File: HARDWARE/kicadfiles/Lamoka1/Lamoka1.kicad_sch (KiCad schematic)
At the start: 6 parts, among them J1 2606-1108/010-000, J2 2606-1352, J3 USB_C_Receptacle_USB2.0_14P, J4 470531000, J5 2604-1103

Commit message: General work on schem, BOM, footprints. Rout 11-14v to 5v buck converter
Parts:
- J3: Manufacturer HRO Electronics -> (none)
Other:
- note added: "This is the output of the transformer,"
- note added: "we will be hooking it up to a NEMA 5-15 plug."
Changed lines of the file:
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@@
 	(rectangle
 		(start 233.426 86.36)
-		(end 279.4 112.522)
+		(end 281.94 118.364)
 		(stroke
 			(width 0)
@@
 		)
 	)
+	(text "This is the output of the transformer, "
+		(exclude_from_sim no)
+		(at 253.238 114.3 0)
+		(effects
+			(font
+				(size 1.27 1.27)
+			)
+		)
+	)
 	(text "Wago-connector 2606-1108/010-000"
 		(exclude_from_sim no)
@@
 		(exclude_from_sim no)
 		(at 152.908 35.814 0)
+		(effects
+			(font
+				(size 1.27 1.27)
+			)
+		)
+	)
+	(text "we will be hooking it up to a NEMA 5-15 plug."
+		(exclude_from_sim no)
+		(at 257.81 116.332 0)
 		(effects
 			(font
@@
 		)
 		(property "Description" ""
+			(at 228.6 54.61 0)
+			(hide yes)
+			(show_name no)
+			(do_not_autoplace no)
+			(effects
+				(font
+					(size 1.27 1.27)
+				)
+			)
+		)
+		(property "KLC_S4.2_DVDD" ""
+			(at 228.6 54.61 0)
+			(hide yes)
+			(show_name no)
+			(do_not_autoplace no)
+			(effects
+				(font
+					(size 1.27 1.27)
+				)
+			)
+		)
+		(property "KLC_S4.2_VREG_LX" ""
 			(at 228.6 54.61 0)
 			(hide yes)
@@
 			)
 		)
-		(property "Manufacturer" "HRO Electronics"
-			(at 29.21 107.95 0)
-			(hide yes)
-			(show_name no)
-			(do_not_autoplace no)
-			(effects
-				(font
-					(size 1.27 1.27)
-				)
-			)
-		)
-		(property "Notes" ""
-			(at 29.21 107.95 0)
-			(hide yes)
-			(show_name no)
-			(do_not_autoplace no)
-			(effects
-				(font
-					(size 1.27 1.27)
-				)
-			)
-		)
 		(property "KLC_S4.2_DVDD" ""
 			(at 29.21 107.95 0)
@@
 			(at 142.24 68.58 0)
 			(hide yes)
+			(show_name no)
+			(do_not_autoplace no)
+			(effects
+				(font
+					(size 1.27 1.27)
+				)
+			)
+		)
+		(property "KLC_S4.2_DVDD" ""
+			(at 142.24 68.58 0)
+			(hide yes)
+			(show_name no)
+			(do_not_autoplace no)
+			(effects
+				(font
+					(size 1.27 1.27)
+				)
+			)
+		)
+		(property "KLC_S4.2_VREG_LX" ""
+			(at 142.24 68.58 0)
+			(hide yes)

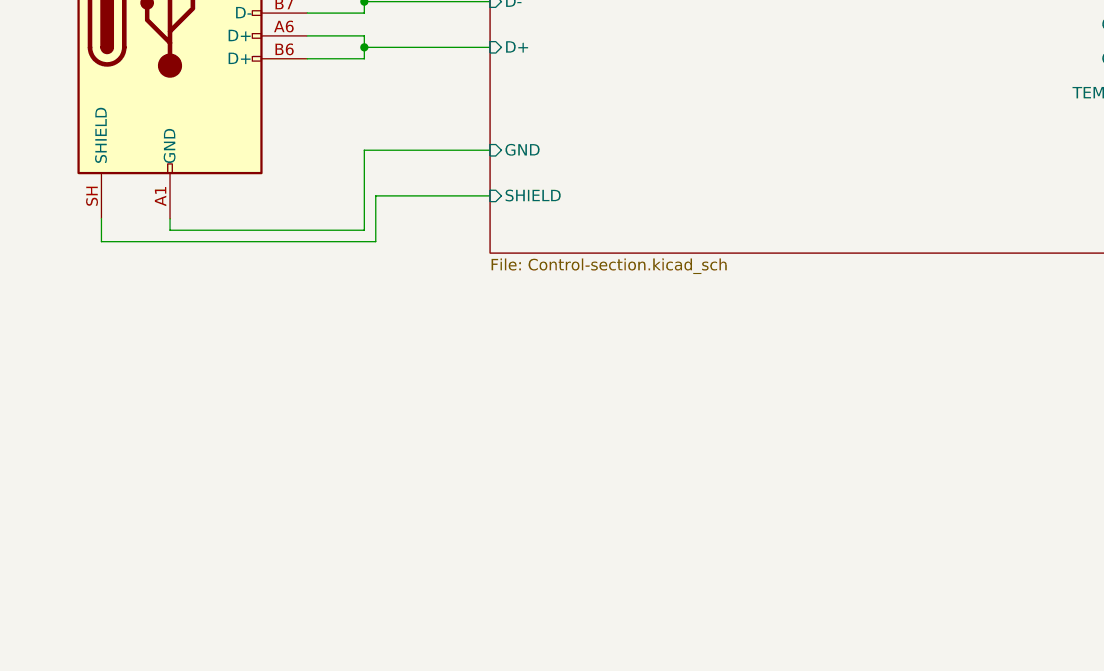
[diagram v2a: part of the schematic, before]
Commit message: ADD seperate user interface board, improve doccumentation
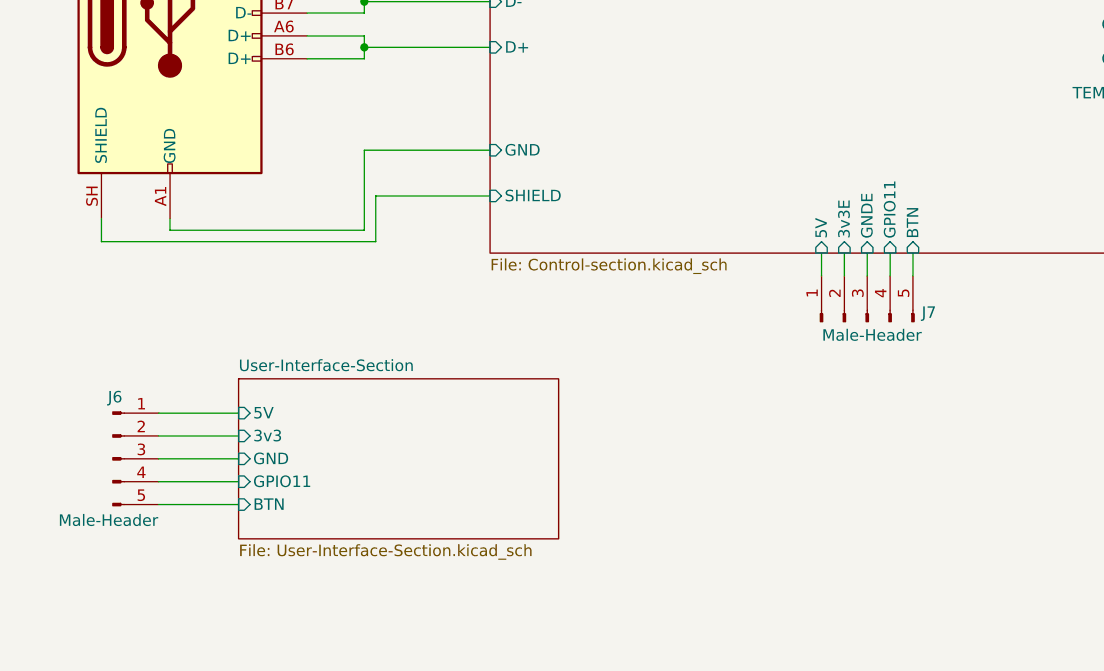
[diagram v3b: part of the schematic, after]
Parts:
- added J6, J7: Male-Header, Connector_PinHeader_2.54mm:PinHeader_1x05_P2.54mm_Vertical_SMD_Pin1Left, symbol Connector:Conn_01x05_Pin
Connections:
- new net Control-Section/3v3E: J7.2 (Pin_2)
- new net Control-Section/5V: J7.1 (Pin_1)
- new net Control-Section/BTN: J7.5 (Pin_5)
- new net Control-Section/GNDE: J7.3 (Pin_3)
- new net Control-Section/GPIO11: J7.4 (Pin_4)
- new net User-Interface-Section/3v3: J6.2 (Pin_2)
- new net User-Interface-Section/5V: J6.1 (Pin_1)
- new net User-Interface-Section/BTN: J6.5 (Pin_5)
- new net User-Interface-Section/GND: J6.3 (Pin_3)
- new net User-Interface-Section/GPIO11: J6.4 (Pin_4)
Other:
- added sheet User-Interface-Section (User-Interface-Section.kicad_sch)
- sheet Control-Section ports: added 3v3E, 5V, BTN, GNDE, GPIO11; removed none

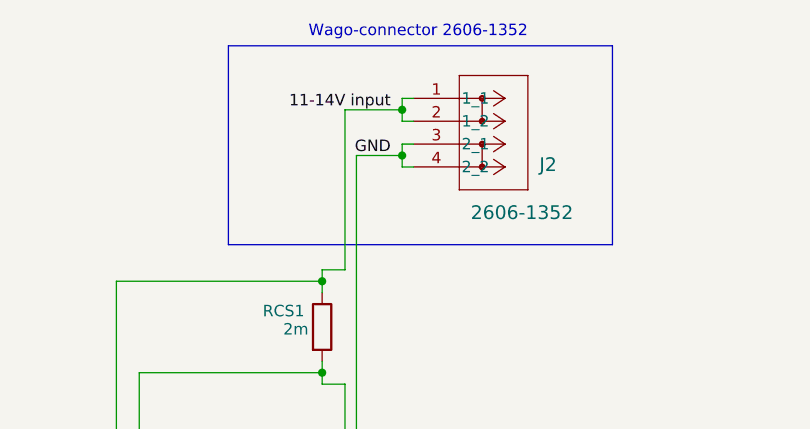
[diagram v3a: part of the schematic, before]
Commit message: Route in pin header for user interface board, and put in connector for fan, other changes as well
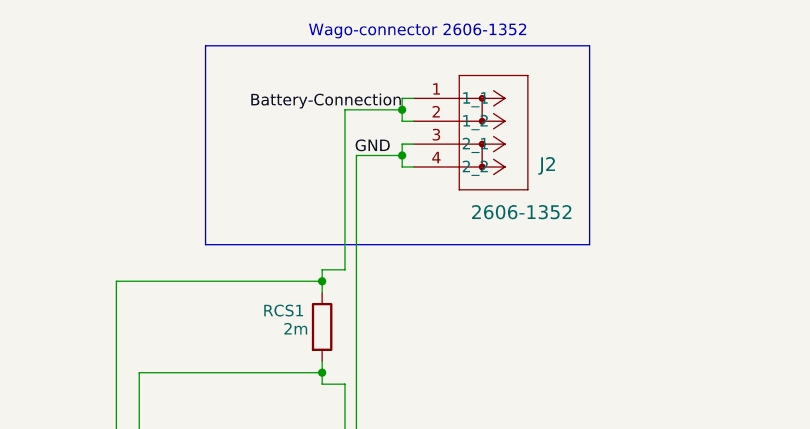
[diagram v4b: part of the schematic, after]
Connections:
- net 11-14V input renamed Battery-Connection 
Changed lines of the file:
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@@
 	)
 	(rectangle
-		(start 131.826 37.338)
-		(end 174.498 59.436)
+		(start 129.286 37.338)
+		(end 171.958 59.436)
 		(stroke
 			(width 0)
@@
 		)
 	)
-	(label "11-14V input"
-		(at 149.86 44.45 180)
-		(effects
-			(font
+	(label "Battery-Connection "
+		(at 151.13 44.45 180)
+		(effects
+			(font
